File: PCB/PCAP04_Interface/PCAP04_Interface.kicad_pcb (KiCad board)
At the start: 2 copper layers, 85 x 78.2 mm, 59 parts, among them IC1 PCAP04-AQFM-24, IC2 PCAP04-AQFM-24, IC3 PCAP04-AQFM-24, J1 Conn_01x04, J2 43045-2022, J3 MEM2067-02-180-00-A, J4 Conn_01x02, U1 PCAP_04-eva-board, U2 ESP-WROOM-32-DEVBOARD

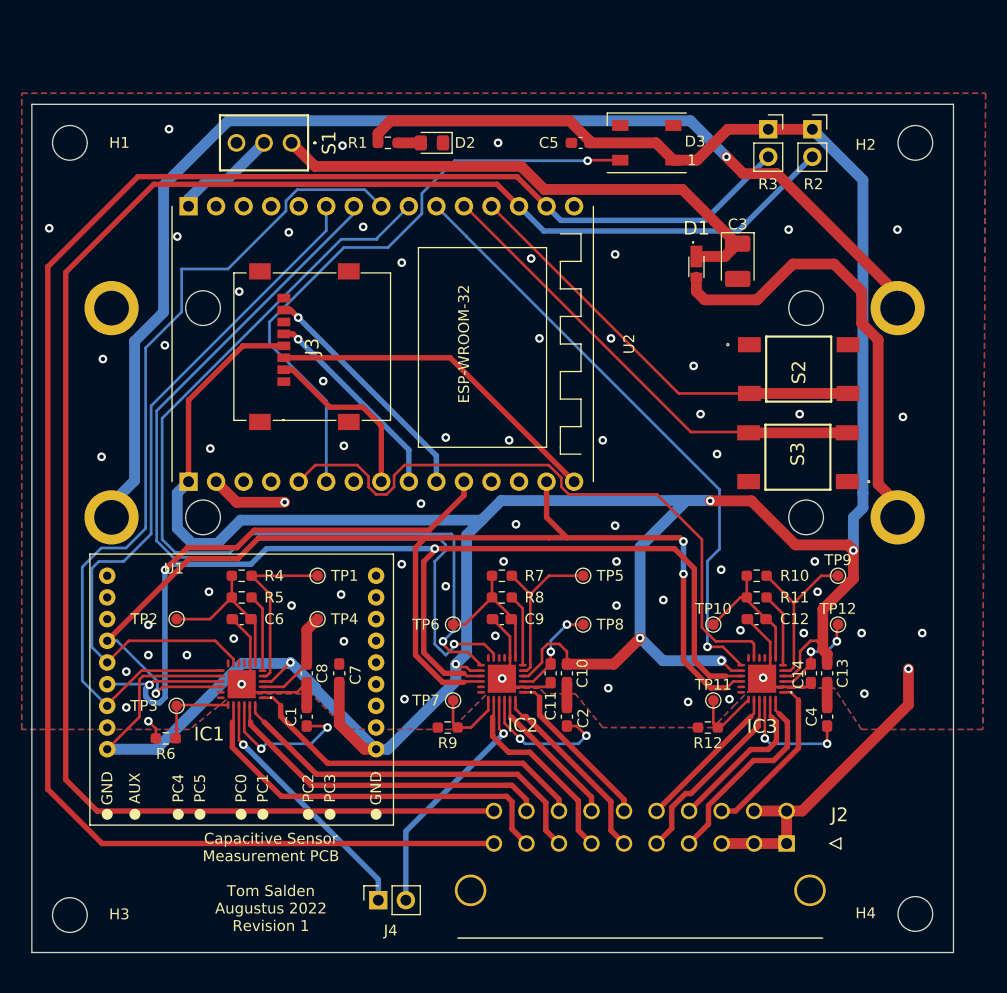
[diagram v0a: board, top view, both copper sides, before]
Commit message: Created PlatformIO-based project
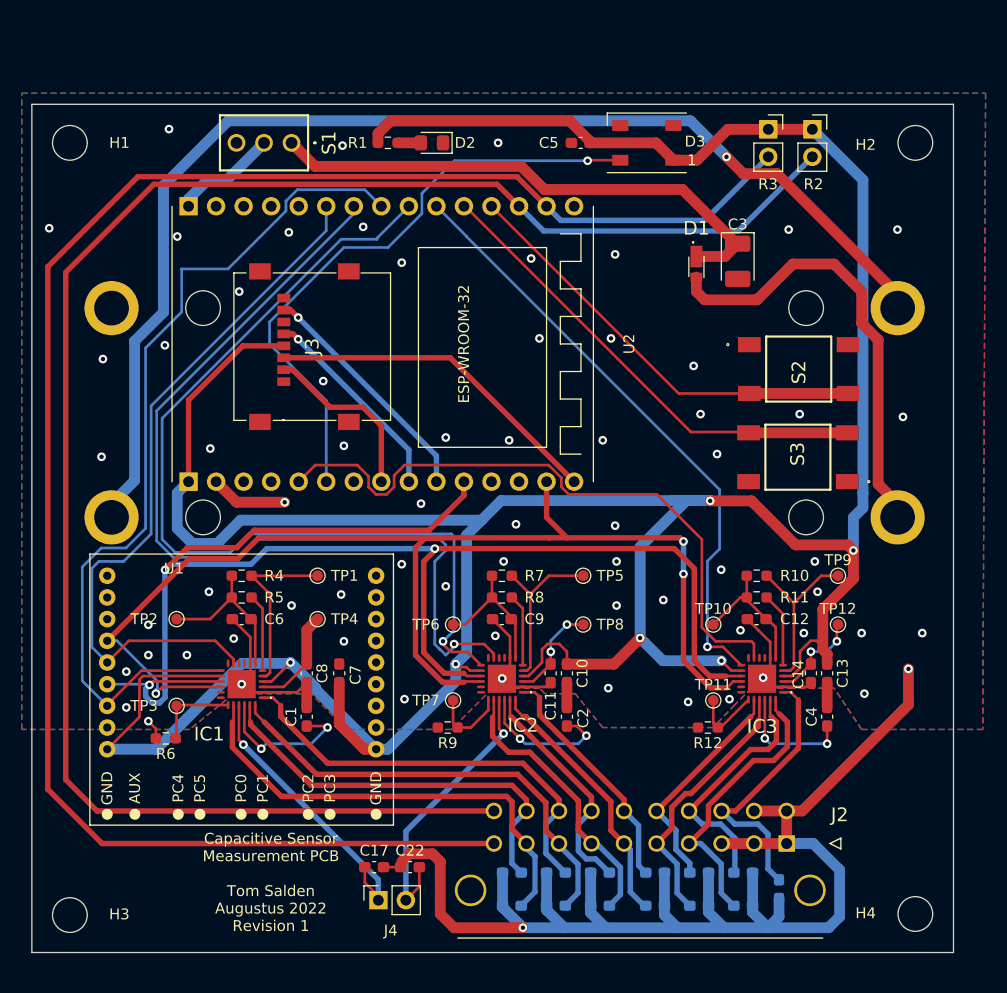
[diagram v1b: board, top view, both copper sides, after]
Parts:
- added C15: C, Capacitor_SMD:C_0603_1608Metric_Pad1.08x0.95mm_HandSolder, B.Cu at (144.3, 141.0)
- added C16: C, Capacitor_SMD:C_0603_1608Metric_Pad1.08x0.95mm_HandSolder, B.Cu at (148.3, 141.0)
- added C17: C, Capacitor_SMD:C_0603_1608Metric_Pad1.08x0.95mm_HandSolder, F.Cu at (131.6, 140.5)
- added C18: C, Capacitor_SMD:C_0603_1608Metric_Pad1.08x0.95mm_HandSolder, B.Cu at (148.3, 144.0)
- added C19: C, Capacitor_SMD:C_0603_1608Metric_Pad1.08x0.95mm_HandSolder, B.Cu at (144.3, 144.0)
- added C20: C, Capacitor_SMD:C_0603_1608Metric_Pad1.08x0.95mm_HandSolder, B.Cu at (152.4, 141.0)
- added C21: C, Capacitor_SMD:C_0603_1608Metric_Pad1.08x0.95mm_HandSolder, B.Cu at (157.5, 141.0)
- added C22: C, Capacitor_SMD:C_0603_1608Metric_Pad1.08x0.95mm_HandSolder, F.Cu at (134.9, 140.5)
- added C23: C, Capacitor_SMD:C_0603_1608Metric_Pad1.08x0.95mm_HandSolder, B.Cu at (157.5, 144.0)
- added C24: C, Capacitor_SMD:C_0603_1608Metric_Pad1.08x0.95mm_HandSolder, B.Cu at (152.4, 144.0)
- added C25: C, Capacitor_SMD:C_0603_1608Metric_Pad1.08x0.95mm_HandSolder, B.Cu at (165.6, 141.0)
- added C26: C, Capacitor_SMD:C_0603_1608Metric_Pad1.08x0.95mm_HandSolder, B.Cu at (168.9, 142.5)
- added C27: C, Capacitor_SMD:C_0603_1608Metric_Pad1.08x0.95mm_HandSolder, B.Cu at (161.5, 144.0)
- added C28: C, Capacitor_SMD:C_0603_1608Metric_Pad1.08x0.95mm_HandSolder, B.Cu at (165.6, 144.0)
- added C29: C, Capacitor_SMD:C_0603_1608Metric_Pad1.08x0.95mm_HandSolder, B.Cu at (161.5, 141.0)
- moved G*** 0.90 mm to (156.0, 125.5)
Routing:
- net GND: track 82.9 -> 178.8 mm, vias 67 -> 68
- net C3.3: track 15.6 -> 25.4 mm
- net C3.2: track 18.6 -> 26.6 mm
- net C3.1: track 14.8 -> 22.7 mm
- net C2.1: track 13.2 -> 21.1 mm
- net C2.4: track 18.2 -> 25.8 mm
- net C1.2: track 35.2 -> 42.3 mm
- net C3.5: track 17.5 -> 24.5 mm
- net C3.4: track 14.0 -> 21.0 mm
- net C1.3: track 32.9 -> 39.8 mm
- net C2.2: track 17.6 -> 24.2 mm
- net C1.1: track 31.2 -> 37.8 mm
- net C1.4: track 36.2 -> 42.8 mm
- net C2.3: track 15.5 -> 22.0 mm
- net C2.5: track 22.4 -> 26.0 mm
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
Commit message: Upgraded webserver functionalities
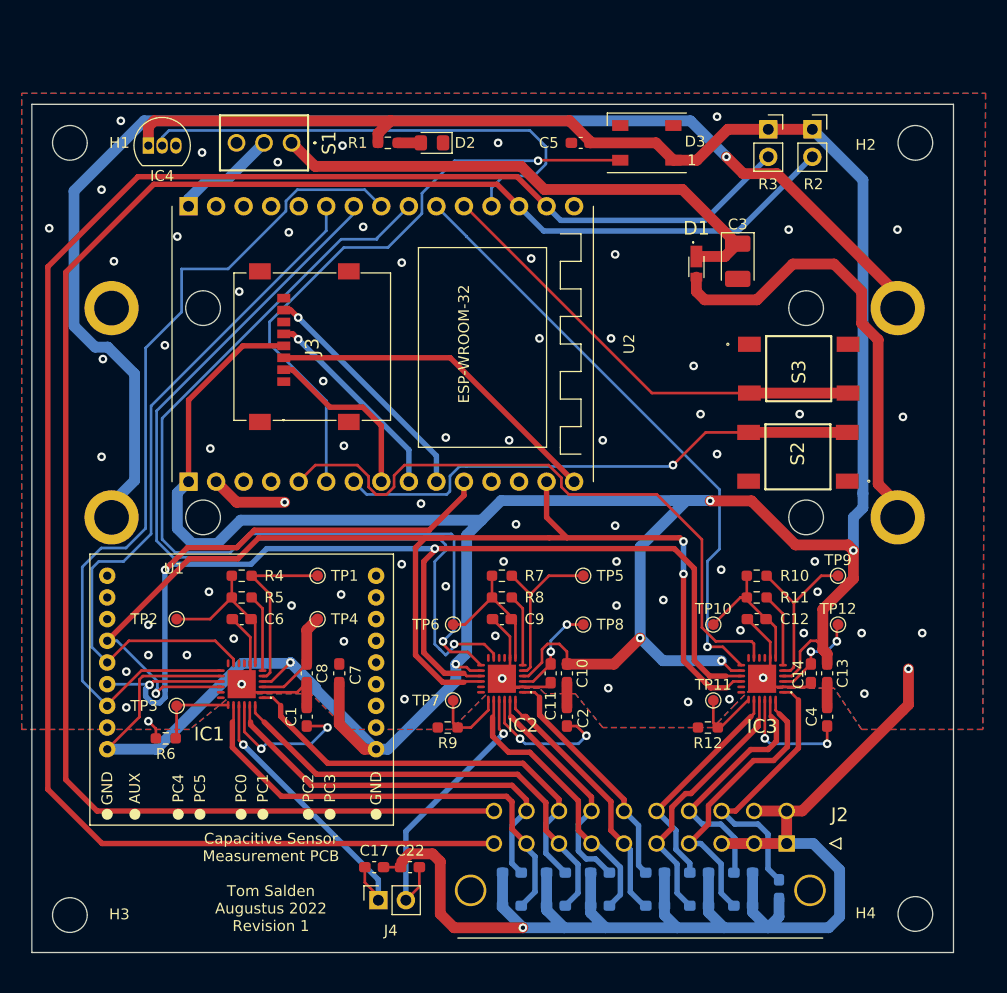
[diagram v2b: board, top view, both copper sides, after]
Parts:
- removed the G*** at (156.0, 125.5)
- added Gr: LOGO, FootrpintLib:TUD_logo, B.Cu at (156.7, 125.7)
- added IC4: MCP9701-E_TO, Package_TO_SOT_THT:TO-92_Inline, F.Cu at (110.7, 73.9)
- moved S3 8.16 mm to (170.7, 94.5), turned to 90 degrees
- moved S2 8.09 mm to (170.7, 102.6), turned to -90 degrees
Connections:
- U2 pad 12: BUTTON1 -> V_TEMP
- U2 pad 22: unconnected-(U2-Pad22) -> BUTTON1
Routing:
- net V_TEMP: track 0.00 -> 46.3 mm
- net +3V3: track 325.1 -> 349.4 mm
- net Net-(J1-Pad2): track 108.1 -> 118.0 mm
- net BUTTON1: track 40.0 -> 49.2 mm, vias 0 -> 1
- net BUTTON2: track 44.0 -> 42.6 mm
- net GND: vias 68 -> 73

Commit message: Poging tot config
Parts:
- removed Gr: LOGO, FootrpintLib:TUD_logo
- added C30: 22u, Capacitor_Tantalum_SMD:CP_EIA-1608-10_AVX-L_Pad1.25x1.05mm_HandSolder, F.Cu at (179.3, 84.5)
- added G***: LOGO, FootrpintLib:TUD_logo, B.Cu at (156.3, 127.0)
- added J5: Conn_02x06_Odd_Even, Connector_PinHeader_2.54mm:PinHeader_2x06_P2.54mm_Vertical, F.Cu at (136.0, 70.0)
- added J6: Conn_02x03_Odd_Even, Connector_PinHeader_2.54mm:PinHeader_2x03_P2.54mm_Vertical, F.Cu at (178.8, 127.8)
- added U3: AMS1117-3.3, Package_TO_SOT_SMD:SOT-223-3_TabPin2, F.Cu at (179.3, 79.4)
- moved H1 5.08 mm to (103.5, 68.6)
- moved H2 5.08 mm to (181.5, 68.6)
- moved C15 1.65 mm to (144.3, 142.6)
- moved C16 1.65 mm to (148.3, 142.6)
- moved C17 1.65 mm to (131.6, 142.1)
- moved C18 1.65 mm to (148.3, 145.7)
- moved C19 1.65 mm to (144.3, 145.7)
- moved C20 1.65 mm to (152.4, 142.6)
- moved C21 1.65 mm to (157.5, 142.6)
- moved C22 1.65 mm to (134.9, 142.1)
- moved C23 1.65 mm to (157.5, 145.7)
- moved C24 1.65 mm to (152.4, 145.7)
- moved C25 1.65 mm to (165.6, 142.6)
- moved C26 1.65 mm to (168.9, 144.1)
- moved C27 1.65 mm to (161.5, 145.7)
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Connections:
- net Net-(J1-Pad2) renamed BM
- D1 pad 2: Net-(D1-Pad2) -> P+
- J1 pad 1: GND -> B-
- J1 pad 4: Net-(D1-Pad2) -> B+
- U2 pad 10: PCAP3_EN -> IO32
- U2 pad 11: BUTTON2 -> I35
- U2 pad 16: +3V3 -> unconnected-(U2-Pad16)
- U2 pad 18: unconnected-(U2-Pad18) -> PCAP3_EN
- U2 pad 21: LED_DATA -> BUTTON1
- U2 pad 22: BUTTON1 -> BUTTON2
- U2 pad 3: unconnected-(U2-Pad3) -> PCAP1_EN
- U2 pad 5: unconnected-(U2-Pad5) -> PCAP2_EN
- U2 pad 8: PCAP1_EN -> LED_DATA
- U2 pad 9: PCAP2_EN -> IO33
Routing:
- net B-: track 0.00 -> 101.9 mm, vias 0 -> 1
- net P+: track 0.00 -> 66.2 mm
- net SD_SCLK: track 18.9 -> 71.4 mm, vias 1 -> 2
- net +6V: track 9.77 -> 57.7 mm, vias 0 -> 1
- net SCL: track 114.3 -> 158.4 mm
- net SDA: track 137.7 -> 180.5 mm
- net SD_MISO: track 22.0 -> 64.4 mm
- net Net-(D1-Pad2): track 40.2 -> 0.00 mm
- net +3V3: track 349.4 -> 384.6 mm, vias 6 -> 7
- net BM: track 118.0 -> 148.9 mm, vias 1 -> 0
- net LED_DATA: track 56.5 -> 28.0 mm
- net SD_MOSI: track 31.5 -> 58.7 mm, vias 0 -> 1
- net B+: track 0.00 -> 18.4 mm
- net I35: track 0.00 -> 18.4 mm
- net IO33: track 0.00 -> 16.2 mm
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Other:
- board size 85 x 78.2 mm -> 85 x 85 mm
- board text added: "3V3"
- board text added: "B+"
- board text added: "B-"
- board text added: "BM"
- board text added: "CIPO"
- board text added: "COPI"
- board text added: "GND"
- board text added: "I35"
- board text added: "IO32"
- board text added: "IO33"
- board text added: "P+"
- board text added: "P-"
- board text added: "SCL"
- board text added: "SCLK"
- board text added: "SDA"
- board text added: "Vbat"
